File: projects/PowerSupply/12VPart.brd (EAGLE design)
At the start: 50 x 50 mm, 26 parts, among them IC1 LM2596T, IC2 LM2596T, X1 IN, X2 OUT

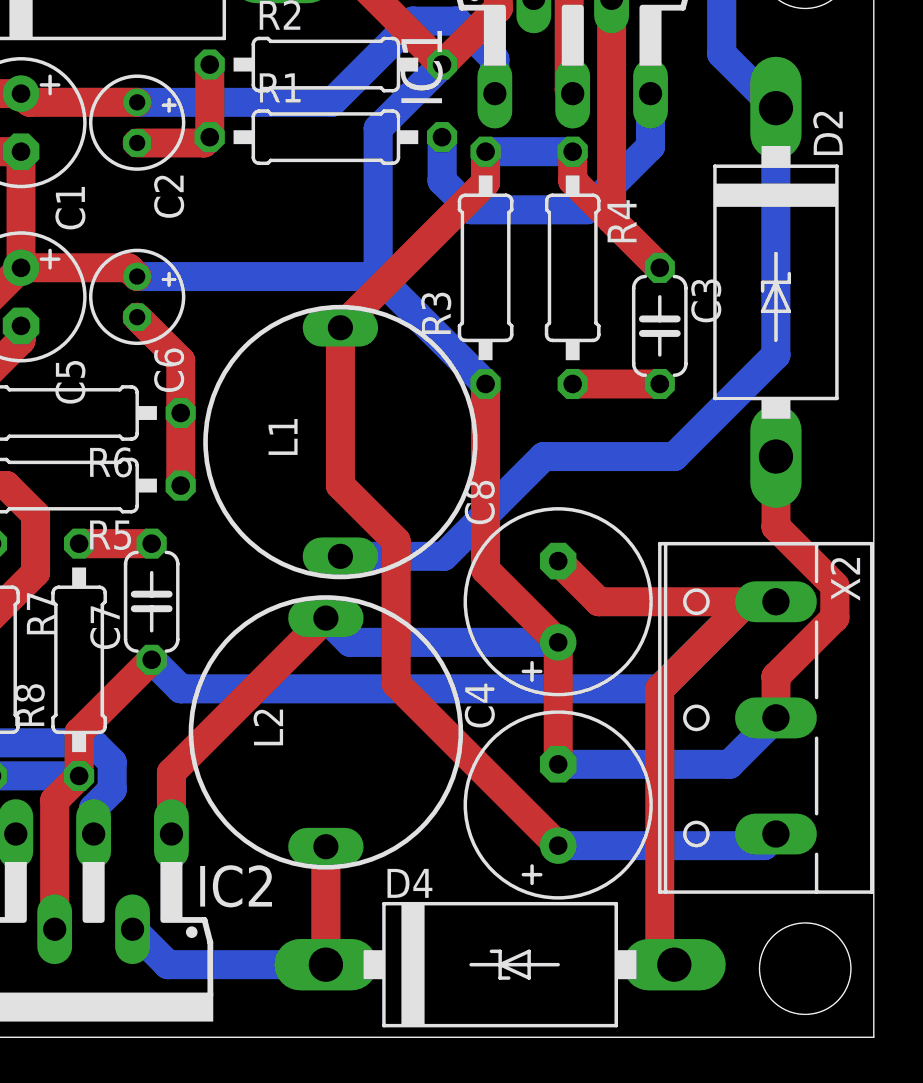
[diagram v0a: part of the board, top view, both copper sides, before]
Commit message: feat: 12 volt part modified
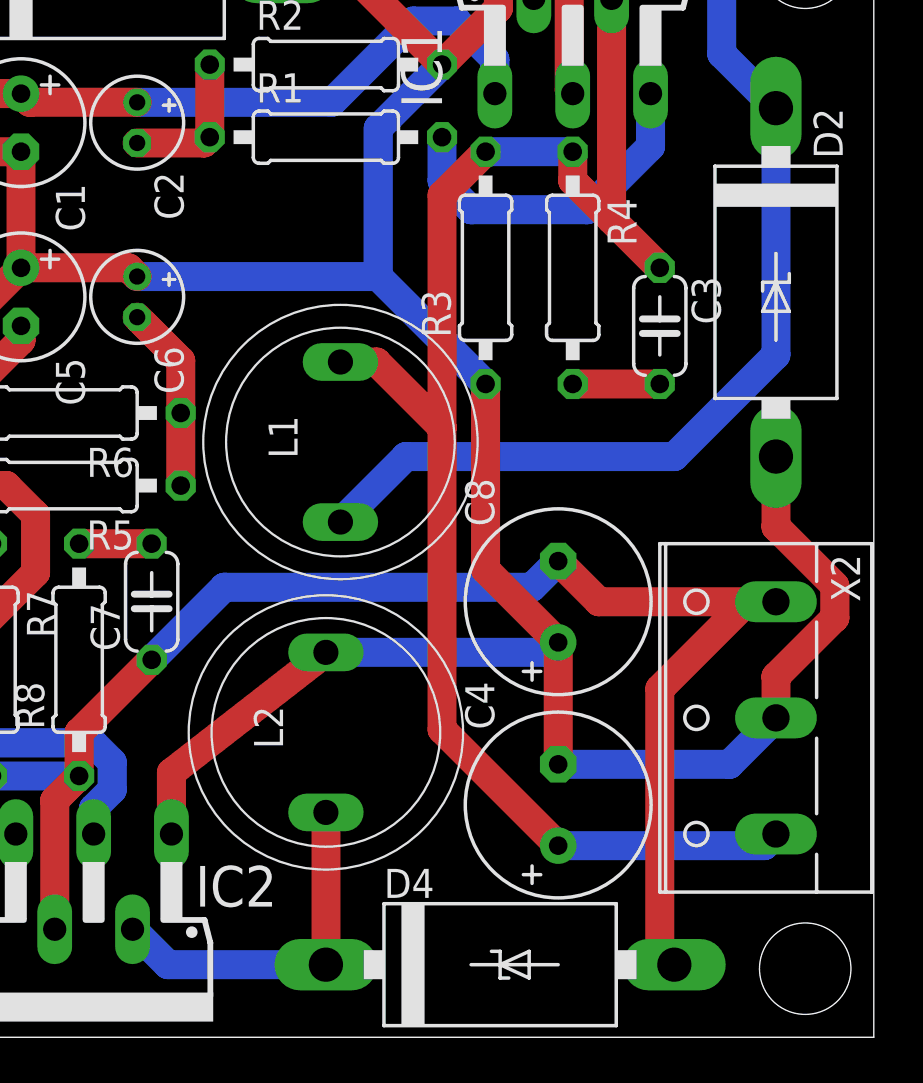
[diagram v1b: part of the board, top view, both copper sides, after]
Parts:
- C4: value 330µF -> 220µF
- L1: device inductor-neosid:SD12-680 -> bb84:IND-120
- L2: value 47µH -> 33µH; device inductor-neosid:SD12-680 -> bb84:IND-120
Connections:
- net +12V: now also L1.P$2; no longer L1.2
- net GND: now also L2.P$2; no longer L2.2
- net N$2: now also L2.P$1; no longer L2.1
- net N$3: now also L1.P$1; no longer L1.1
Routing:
- net -12V: track 74.7 -> 64.9 mm
- net +12V: track 69.8 -> 71.7 mm
- net N$2: track 14.3 -> 15.8 mm
- net GND: track 155.9 -> 154.7 mm
- net N$3: track 51.4 -> 50.8 mm
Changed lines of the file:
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@@
 <attribute name="VALUE" x="37.973" y="33.274" size="1.27" layer="27" ratio="10" rot="R270"/>
 </element>
-<element name="C4" library="rcl" library_urn="urn:adsk.eagle:library:334" package="E3,5-8" package3d_urn="urn:adsk.eagle:package:23360/2" value="330µF" x="36.195" y="10.16" smashed="yes" rot="R90">
+<element name="C4" library="rcl" library_urn="urn:adsk.eagle:library:334" package="E3,5-8" package3d_urn="urn:adsk.eagle:package:23360/2" value="220µF" x="36.195" y="10.16" smashed="yes" rot="R90">
 <attribute name="NAME" x="33.401" y="13.462" size="1.27" layer="25" ratio="10" rot="R90"/>
 <attribute name="POPULARITY" value="13" x="66.675" y="29.21" size="1.778" layer="27" rot="R90" display="off"/>
@@
 <attribute name="VALUE" x="0.635" y="5.08" size="1.778" layer="27" ratio="10"/>
 </element>
-<element name="L1" library="inductor-neosid" library_urn="urn:adsk.eagle:library:241" package="SD12-680" package3d_urn="urn:adsk.eagle:package:14657/1" value="33µH" x="26.67" y="26.035" smashed="yes" rot="R90">
-<attribute name="MF" value="BUSSMANN" x="33.02" y="45.085" size="1.778" layer="27" rot="R90" display="off"/>
-<attribute name="MPN" value="SD12-680" x="33.02" y="45.085" size="1.778" layer="27" rot="R90" display="off"/>
+<element name="L1" library="bb84" package="IND-120" value="33µH" x="26.67" y="26.035" smashed="yes" rot="R90">
 <attribute name="NAME" x="24.797" y="25.317" size="1.27" layer="25" rot="R90"/>
-<attribute name="OC_FARNELL" value="unknown" x="33.02" y="45.085" size="1.778" layer="27" rot="R90" display="off"/>
-<attribute name="OC_NEWARK" value="19K7201" x="33.02" y="45.085" size="1.778" layer="27" rot="R90" display="off"/>
-<attribute name="POPULARITY" value="0" x="33.02" y="45.085" size="1.778" layer="27" rot="R90" display="off"/>
 <attribute name="VALUE" x="29.67" y="24.055" size="1.27" layer="27" rot="R90"/>
 </element>
-<element name="L2" library="inductor-neosid" library_urn="urn:adsk.eagle:library:241" package="SD12-680" package3d_urn="urn:adsk.eagle:package:14657/1" value="47µH" x="26.035" y="13.335" smashed="yes" rot="R90">
-<attribute name="MF" value="BUSSMANN" x="32.385" y="45.085" size="1.778" layer="27" rot="R90" display="off"/>
-<attribute name="MPN" value="SD12-680" x="32.385" y="45.085" size="1.778" layer="27" rot="R90" display="off"/>
+<element name="L2" library="bb84" package="IND-120" value="33µH" x="26.035" y="13.335" smashed="yes" rot="R90">
 <attribute name="NAME" x="24.162" y="12.617" size="1.27" layer="25" rot="R90"/>
-<attribute name="OC_FARNELL" value="unknown" x="32.385" y="45.085" size="1.778" layer="27" rot="R90" display="off"/>
-<attribute name="OC_NEWARK" value="19K7201" x="32.385" y="45.085" size="1.778" layer="27" rot="R90" display="off"/>
-<attribute name="POPULARITY" value="0" x="32.385" y="45.085" size="1.778" layer="27" rot="R90" display="off"/>
 <attribute name="VALUE" x="29.035" y="10.085" size="1.27" layer="27" rot="R90"/>
 </element>
@@
 <contactref element="R3" pad="1"/>
 <contactref element="D2" pad="A"/>
-<contactref element="L2" pad="2"/>
+<contactref element="L2" pad="P$2"/>
 <contactref element="R7" pad="1"/>
 <contactref element="C8" pad="+"/>
@@
 <wire x1="7.62" y1="21.59" x2="11.43" y2="21.59" width="1.27" layer="1"/>
 <wire x1="19.2786" y1="8.89" x2="19.2786" y2="11.5786" width="1.27" layer="1"/>
-<wire x1="19.2786" y1="11.5786" x2="26.035" y2="18.335" width="1.27" layer="1"/>
+<wire x1="19.2786" y1="11.5786" x2="26.035" y2="16.835" width="1.27" layer="1"/>
 <wire x1="36.195" y1="11.938" x2="36.195" y2="17.272" width="1.27" layer="1"/>
 <wire x1="36.195" y1="17.272" x2="33.02" y2="20.447" width="1.27" layer="1"/>
@@
 <wire x1="36.195" y1="11.938" x2="43.688" y2="11.938" width="1.27" layer="16"/>
 <wire x1="43.688" y1="11.938" x2="45.72" y2="13.97" width="1.27" layer="16"/>
-<wire x1="36.195" y1="17.272" x2="27.098" y2="17.272" width="1.27" layer="16"/>
-<wire x1="27.098" y1="17.272" x2="26.035" y2="18.335" width="1.27" layer="16"/>
 <wire x1="17.78" y1="33.274" x2="28.321" y2="33.274" width="1.27" layer="16"/>
 <wire x1="28.321" y1="33.274" x2="33.02" y2="28.575" width="1.27" layer="16"/>
 <wire x1="31.115" y1="42.545" x2="28.321" y2="39.751" width="1.27" layer="16"/>
 <wire x1="28.321" y1="39.751" x2="28.321" y2="33.274" width="1.27" layer="16"/>
+<wire x1="36.195" y1="17.272" x2="35.758" y2="16.835" width="1.27" layer="16"/>
+<wire x1="35.758" y1="16.835" x2="26.035" y2="16.835" width="1.27" layer="16"/>
 </signal>
 <signal name="N$3">
 <contactref element="IC1" pad="2"/>
 <contactref element="D2" pad="C"/>
-<contactref element="L1" pad="1"/>
-<wire x1="26.67" y1="21.035" x2="31.195" y2="21.035" width="1.27" layer="16"/>
-<wire x1="31.195" y1="21.035" x2="35.56" y2="25.4" width="1.27" layer="16"/>
-<wire x1="35.56" y1="25.4" x2="41.275" y2="25.4" width="1.27" layer="16"/>
-<wire x1="41.275" y1="25.4" x2="45.72" y2="29.845" width="1.27" layer="16"/>
+<contactref element="L1" pad="P$1"/>
+<wire x1="45.72" y1="29.845" x2="41.275" y2="25.4" width="1.27" layer="16"/>
 <wire x1="45.72" y1="29.845" x2="45.72" y2="40.64" width="1.27" layer="16"/>
 <wire x1="45.72" y1="40.64" x2="43.349" y2="43.011" width="1.27" layer="16"/>
@@
 <wire x1="36.83" y1="48.26" x2="35.1282" y2="46.5582" width="1.27" layer="16"/>
 <wire x1="35.1282" y1="46.5582" x2="35.1282" y2="45.4406" width="1.27" layer="16"/>
+<wire x1="29.535" y1="25.4" x2="26.67" y2="22.535" width="1.27" layer="16"/>
+<wire x1="41.275" y1="25.4" x2="29.535" y2="25.4" width="1.27" layer="16"/>
 </signal>
 <signal name="N$2">
-<contactref element="L2" pad="1"/>
+<contactref element="L2" pad="P$1"/>
 <contactref element="IC2" pad="2"/>
 <contactref element="D4" pad="C"/>
-<wire x1="26.035" y1="3.175" x2="26.035" y2="8.335" width="1.27" layer="1"/>
+<wire x1="26.035" y1="3.175" x2="26.035" y2="9.835" width="1.27" layer="1"/>
 <wire x1="26.035" y1="3.175" x2="19.1262" y2="3.175" width="1.27" layer="16"/>
 <wire x1="19.1262" y1="3.175" x2="17.5768" y2="4.7244" width="1.27" layer="16"/>
@@
 <contactref element="R4" pad="1"/>
 <contactref element="C3" pad="1"/>
-<contactref element="L1" pad="2"/>
+<contactref element="L1" pad="P$2"/>
 <contactref element="C4" pad="+"/>
 <wire x1="40.64" y1="33.655" x2="36.83" y2="37.465" width="1.27" layer="1"/>
@@
 <wire x1="38.5318" y1="45.4406" x2="38.5318" y2="35.7632" width="1.27" layer="1"/>
 <wire x1="38.5318" y1="35.7632" x2="40.64" y2="33.655" width="1.27" layer="1"/>
-<wire x1="33.02" y1="38.735" x2="33.02" y2="37.385" width="1.27" layer="1"/>
-<wire x1="33.02" y1="37.385" x2="26.67" y2="31.035" width="1.27" layer="1"/>
-<wire x1="26.67" y1="31.035" x2="26.67" y2="24.14028125" width="1.27" layer="1"/>
-<wire x1="26.67" y1="24.14028125" x2="29.1074" y2="21.70288125" width="1.27" layer="1"/>
-<wire x1="29.1074" y1="15.4696" x2="36.195" y2="8.382" width="1.27" layer="1"/>
-<wire x1="29.1074" y1="21.70288125" x2="29.1074" y2="15.4696" width="1.27" layer="1"/>
 <wire x1="45.212" y1="8.382" x2="36.195" y2="8.382" width="1.27" layer="16"/>
 <wire x1="33.02" y1="38.735" x2="36.83" y2="38.735" width="1.27" layer="16"/>
 <wire x1="45.72" y1="8.89" x2="45.212" y2="8.382" width="1.27" layer="16"/>
+<wire x1="36.195" y1="8.382" x2="31.115" y2="13.462" width="1.27" layer="1"/>
+<wire x1="31.115" y1="13.462" x2="31.115" y2="26.67" width="1.27" layer="1"/>
+<wire x1="28.25" y1="29.535" x2="31.115" y2="26.67" width="1.27" layer="1"/>
+<wire x1="28.25" y1="29.535" x2="26.67" y2="29.535" width="1.27" layer="1"/>
+<wire x1="31.115" y1="26.67" x2="31.115" y2="36.83" width="1.27" layer="1"/>
+<wire x1="31.115" y1="36.83" x2="33.02" y2="38.735" width="1.27" layer="1"/>
 </signal>
 <signal name="-12V">
@@
 <wire x1="15.24" y1="13.335" x2="18.415" y2="16.51" width="1.27" layer="1"/>
 <wire x1="11.43" y1="11.43" x2="15.24" y2="11.43" width="1.27" layer="16"/>
-<wire x1="18.415" y1="16.51" x2="19.685" y2="15.24" width="1.27" layer="16"/>
 <wire x1="36.195" y1="20.828" x2="37.973" y2="19.05" width="1.27" layer="1"/>
-<wire x1="44.45" y1="19.05" x2="40.64" y2="15.24" width="1.27" layer="16"/>
-<wire x1="19.685" y1="15.24" x2="40.64" y2="15.24" width="1.27" layer="16"/>
 <wire x1="41.275" y1="3.175" x2="40.64" y2="3.81" width="1.27" layer="1"/>
 <wire x1="40.64" y1="3.81" x2="40.64" y2="15.24" width="1.27" layer="1"/>
 <wire x1="37.973" y1="19.05" x2="44.45" y2="19.05" width="1.27" layer="1"/>
 <wire x1="44.45" y1="19.05" x2="45.72" y2="19.05" width="1.27" layer="1"/>
-<wire x1="45.72" y1="19.05" x2="44.45" y2="19.05" width="1.27" layer="16"/>
 <wire x1="40.64" y1="15.24" x2="44.45" y2="19.05" width="1.27" layer="1"/>
+<wire x1="18.415" y1="16.51" x2="21.59" y2="19.685" width="1.27" layer="16"/>
+<wire x1="35.052" y1="19.685" x2="36.195" y2="20.828" width="1.27" layer="16"/>
+<wire x1="21.59" y1="19.685" x2="35.052" y2="19.685" width="1.27" layer="16"/>
 </signal>
 </signals>

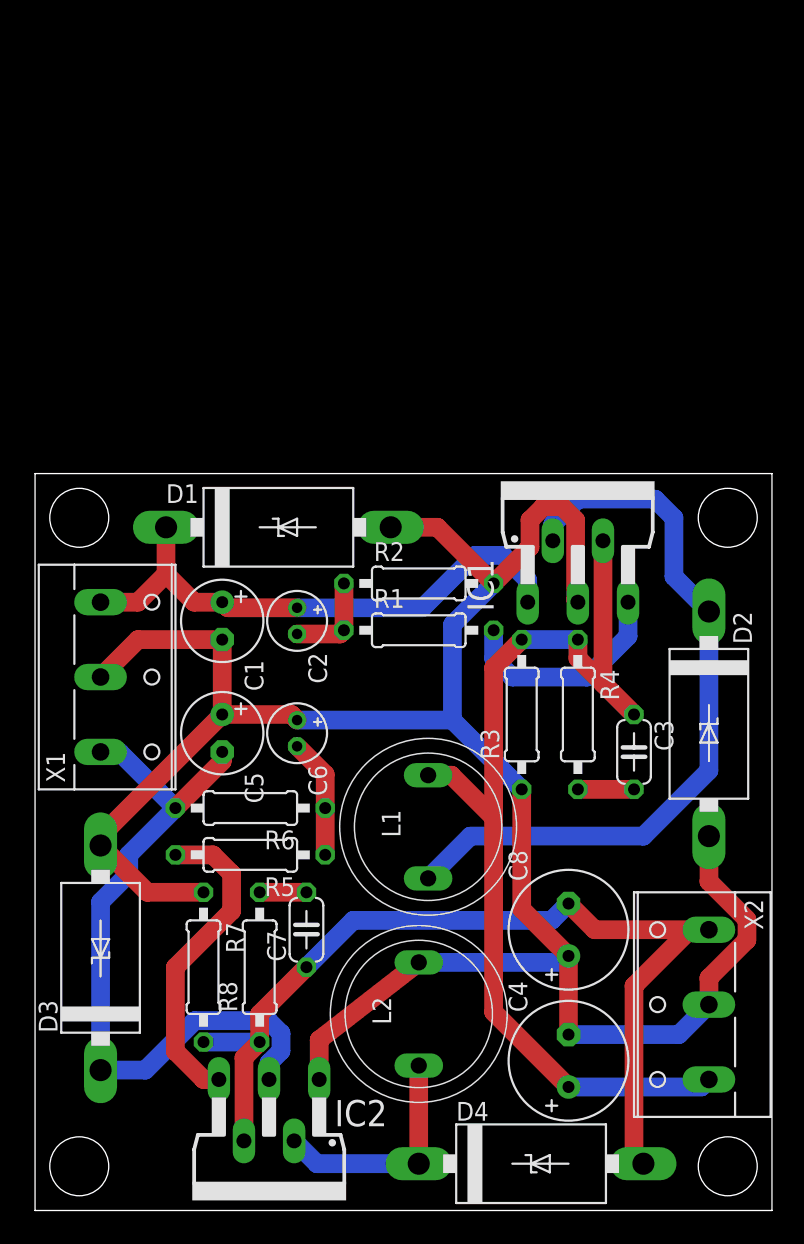
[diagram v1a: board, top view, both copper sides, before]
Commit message: feat: modified 12 volt parts
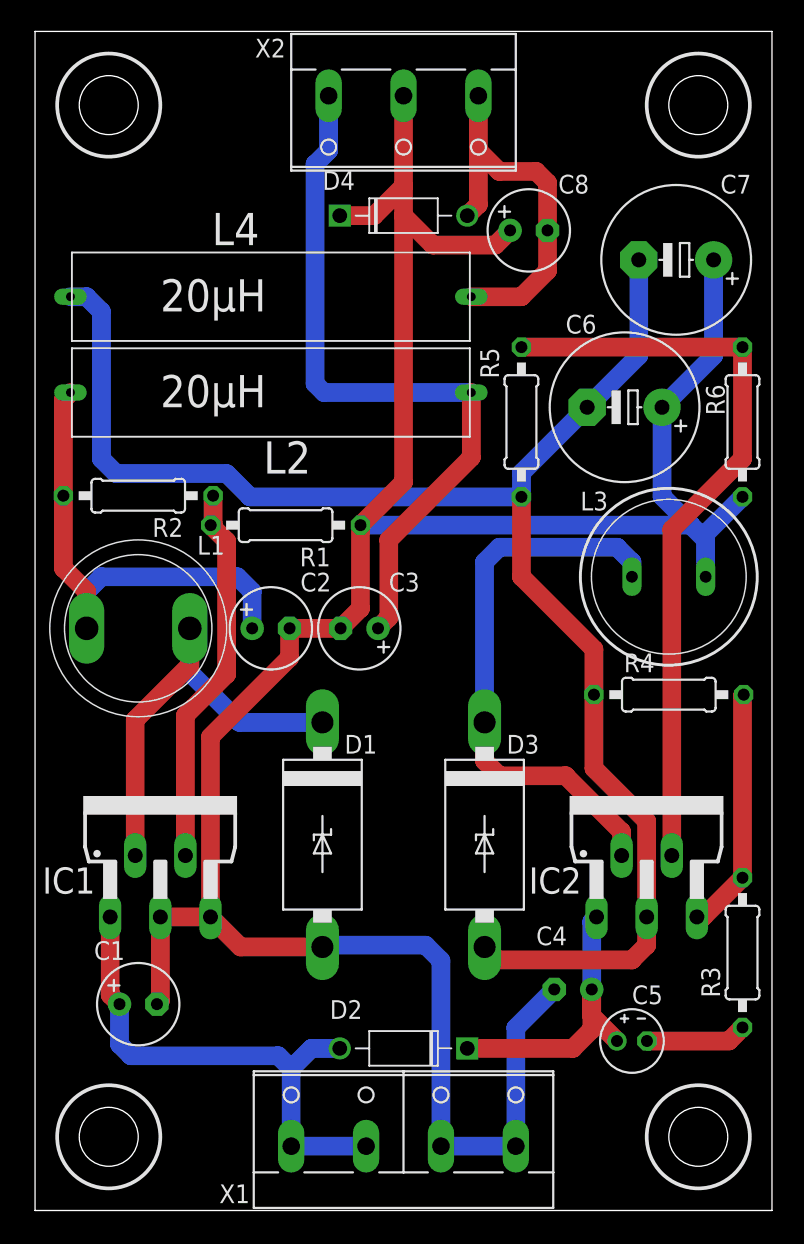
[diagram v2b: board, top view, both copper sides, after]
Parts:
- removed R7: 1k, rcl:0207/10
- removed R8: 8.87k, rcl:0207/10
- added L3: 220µH, bb84:11PHC
- added L4: 20µH, bb84:B82111B
- C2: value 0.1µF -> 220µF; device rcl:E1,8-4 -> rcl:E2,5-6
- C3: value 390pF -> 100µF; device rcl:C050-024X044 -> rcl:E2,5-6
- C4: value 220µF -> 100µF; device rcl:E3,5-8 -> rcl:E2,5-6
- C5: value 100µF -> 0.1µF; device rcl:E2,5-6 -> rcl:E2-4
- C6: value 0.1µF -> 1000µF; device rcl:E1,8-4 -> rcl:E5-10,5
- C7: value 390pF -> 1000µF; device rcl:C050-024X044 -> rcl:E5-10,5
- C8: value 470µF -> 100µF; device rcl:E3,5-8 -> rcl:E2,5-6
- D2, D4: value 1N5822 -> 1N4007; device diode:C4111-15 -> Diodes:DO-41
- L2: value 33µH -> 20µH; device bb84:IND-120 -> bb84:B82111B
- R1, R5: value 47k -> 1k
- R2, R6: value 47k -> 8.87k
- R3: value 1k -> 47k
- R4: value 8.87k -> 47k
- X1: value IN -> PWR-IN; device con-wago-508:W237-133 -> con-wago-508:W237-4P
- X2: value OUT -> PWR-OUT
- moved D4 64.9 mm to (25.0, 67.5)
- moved X2 64.3 mm to (25.0, 75.0), turned to 180 degrees
- moved C7 51.9 mm to (43.5, 64.5), turned to 180 degrees
- moved C8 47.5 mm to (33.5, 66.5), turned to 0 degrees
- moved L2 43.3 mm to (16.0, 55.5), turned to 0 degrees
- moved R6 42.4 mm to (48.0, 53.5), turned to 270 degrees
- moved X1 37.0 mm to (25.0, 5.00), turned to 0 degrees
- moved IC1 35.5 mm to (8.50, 25.0)
- moved C5 34.8 mm to (40.5, 11.5), turned to 0 degrees
- moved R5 34.7 mm to (33.0, 53.5), turned to 90 degrees
- moved IC2 33.3 mm to (41.5, 25.0), turned to 0 degrees
- moved C6 31.3 mm to (40.0, 54.5), turned to 180 degrees
- moved D2 30.2 mm to (25.0, 11.0), turned to 180 degrees
- moved D3 27.4 mm to (30.5, 25.5), turned to 270 degrees
- moved C1 26.6 mm to (7.00, 14.0), turned to 0 degrees
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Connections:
- removed net +12V: C3.1, C4.+, IC1.4, L1.P$2, R3.2, R4.1, X2.1
- removed net +20V: C1.+, C2.+, D1.C, IC1.1, X1.1
- removed net -12V: C7.1, C8.-, D4.A, IC2.4, R7.2, R8.1, X2.3
- removed net -20V: C5.-, D3.C, IC2.3, R6.2, X1.3
- removed net N$2: D4.C, IC2.2, L2.P$1
- removed net N$8: C6.-, R5.1, R6.1
- new net N$10: IC2.5, R3.2, R4.2
- new net N$11: C6.-, C7.-, D3.A, IC2.3, L4.P$1, R4.1, R5.1
- new net N$12: D3.C, IC2.2, L3.P$1
- new net N$14: IC2.4, R5.2, R6.1
- new net N$9: C5.-, R3.1
- new net VCC: C1.+, D2.A, IC1.1, X1.1, X1.2
- net GND: now also C2.-, C3.-, C7.+, D4.C, IC1.5, L3.P$2, R1.1, R6.2, X1.3, X1.4; no longer C5.+, D2.A, D3.A, IC2.1, L2.P$2, R2.2, R3.1, R7.1, X1.2
- net N$1: now also C4.+, C5.+, D2.C, IC2.1; no longer C3.2, R4.2
- net N$3: now also C8.-, D4.A, L4.P$2, X2.1; no longer D2.C, IC1.2, L1.P$1
- net N$4: now also D1.C, IC1.2, L1.P$1; no longer IC1.5, R1.2
- net N$5: now also IC1.4, R1.2, R2.1; no longer C7.2, R8.2
- net N$6: now also C2.+, L1.P$2, L2.P$1, R2.2; no longer C2.-, R1.1, R2.1
- net N$7: now also C3.+, L2.P$2, X2.3; no longer IC2.5, R5.2
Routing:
- net N$11: track 0.00 -> 107.2 mm
- net +12V: track 71.7 -> 0.00 mm
- net -12V: track 64.9 -> 0.00 mm
- net N$14: track 0.00 -> 51.5 mm
- net -20V: track 49.1 -> 0.00 mm
- net N$12: track 0.00 -> 38.2 mm
- net +20V: track 38.2 -> 0.00 mm
- net VCC: track 0.00 -> 35.4 mm
- net GND: track 154.7 -> 183.1 mm
- net N$7: track 21.7 -> 49.4 mm
- net N$6: track 6.46 -> 33.9 mm
- net N$3: track 50.8 -> 25.9 mm
- net N$5: track 3.17 -> 26.1 mm
- net N$1: track 3.81 -> 21.0 mm
- net N$10: track 0.00 -> 16.7 mm
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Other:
- board size 50 x 50 mm -> 50 x 80 mm
